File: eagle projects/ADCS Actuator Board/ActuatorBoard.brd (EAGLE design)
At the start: 91 x 91 mm, 278 parts, among them J19 TE_1-84953-1, J20 TE_1-84953-1, J21 TE_1-84953-1, U10 DRV10970_MOTOR_DRIVERDRV10970, U12 DRV10970_MOTOR_DRIVERDRV10970, U13 ADS7841E_2K5, U15 TLV9051IDCKR, U19 TLV9051IDCKR, U2 ADS7841E_2K5, U21 TLV9051IDCKR, U23 TLV9051IDCKR, U24 TLV9051IDCKR, U25 ADS7841E_2K5, U26 TLV9051IDCKR, U27 ADS7841E_2K5, U28 TLV9051IDCKR, U29 TLV9051IDCKR, U3 ADS7841E_2K5, U30 TLV9051IDCKR, U31 TLV9051IDCKR, U32 TLV9051IDCKR, U34 TVS991, U35 BD6210F-E2, U38 TVS991, U39 BD6210F-E2, U4 ADS7841E_2K5, U5 TVS991, U6 TLV9051IDCKR, U7 DRV10970_MOTOR_DRIVERDRV10970, U9 BD6210F-E2

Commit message: minor layout tweaks
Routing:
- net GND: vias 170 -> 172
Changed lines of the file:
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@@
 <setting verticaltext="up"/>
 </settings>
-<grid distance="1" unitdist="mil" unit="mil" style="lines" multiple="1" display="yes" altdistance="12.5" altunitdist="mil" altunit="mm"/>
+<grid distance="50" unitdist="mil" unit="mil" style="lines" multiple="1" display="yes" altdistance="12.5" altunitdist="mil" altunit="mil"/>
 <layers>
 <layer number="1" name="Top" color="4" fill="1" visible="yes" active="yes"/>
@@
 </layers>
 <board>
-<fusionsync huburn="a.YnVzaW5lc3M6bXlkYWwyMA" projecturn="a.YnVzaW5lc3M6bXlkYWwyMCMyMDIxMDExNjM3MjQwMzc3Ng" f3durn="urn:adsk.wipprod:dm.lineage:TKW3tc-mS0qsFWWO9AN0Ug" pcbguid="" lastpulledtime="" lastsyncedchangeguid="" latestrevisionid="0074a831-43cd-42bd-b3bd-cc89c6651567" lastsyncedrevisionid="0074a831-43cd-42bd-b3bd-cc89c6651567" lastboardhashguid="857bcac5-dcdf-7e34-be52-16fdd3c31308" lastpushedtime="2021-02-03T02:47:48Z" linktopcb3d="false"/>
+<fusionsync huburn="a.YnVzaW5lc3M6bXlkYWwyMA" projecturn="a.YnVzaW5lc3M6bXlkYWwyMCMyMDIxMDExNjM3MjQwMzc3Ng" f3durn="urn:adsk.wipprod:dm.lineage:TKW3tc-mS0qsFWWO9AN0Ug" pcbguid="" lastpulledtime="2021-02-14T18:09:55Z" lastsyncedchangeguid="" latestrevisionid="c2152030-a1ea-4700-91c3-66171d633219" lastsyncedrevisionid="c2152030-a1ea-4700-91c3-66171d633219" lastboardhashguid="a1286e25-3132-5004-a41b-18cce8fad25a" lastpushedtime="2021-02-14T18:11:04Z" linktopcb3d="true"/>
 <plain>
-<wire x1="0" y1="0" x2="31.5" y2="0" width="0.1524" layer="20" locked="yes"/>
-<wire x1="31.5" y1="0" x2="31.5" y2="7" width="0.1524" layer="20" locked="yes"/>
-<wire x1="31.5" y1="7" x2="59.5" y2="7" width="0.1524" layer="20" locked="yes"/>
-<wire x1="59.5" y1="7" x2="59.5" y2="0" width="0.1524" layer="20" locked="yes"/>
-<wire x1="59.5" y1="0" x2="91" y2="0" width="0.1524" layer="20" locked="yes"/>
-<wire x1="91" y1="0" x2="91" y2="42" width="0.1524" layer="20" locked="yes"/>
-<wire x1="91" y1="42" x2="87" y2="42" width="0.1524" layer="20" locked="yes"/>
-<wire x1="87" y1="42" x2="87" y2="80" width="0.1524" layer="20" locked="yes"/>
-<wire x1="87" y1="80" x2="91" y2="80" width="0.1524" layer="20" locked="yes"/>
-<wire x1="91" y1="80" x2="91" y2="91" width="0.1524" layer="20" locked="yes"/>
-<wire x1="91" y1="91" x2="0" y2="91" width="0.1524" layer="20" locked="yes"/>
-<wire x1="0" y1="91" x2="0" y2="80" width="0.1524" layer="20" locked="yes"/>
-<wire x1="0" y1="80" x2="4" y2="80" width="0.1524" layer="20" locked="yes"/>
-<wire x1="4" y1="80" x2="4" y2="42" width="0.1524" layer="20" locked="yes"/>
-<wire x1="4" y1="42" x2="0" y2="42" width="0.1524" layer="20" locked="yes"/>
-<wire x1="0" y1="42" x2="0" y2="0" width="0.1524" layer="20" locked="yes"/>
 <text x="64.6176" y="16.4719" size="1.016" layer="51" font="vector" rot="R90">ACTUATOR BOARD - REV A</text>
 <text x="65.9511" y="16.4719" size="1.016" layer="151" font="vector" rot="R90">Dalhousie Space Systems Lab</text>
@@
 <rectangle x1="72.6059" y1="66.3067" x2="73.2155" y2="66.3321" locked="yes" layer="203" rot="R180" grouprefs="BOTTOM_LOGO"/>
 <rectangle x1="72.8091" y1="66.3321" x2="73.0631" y2="66.3575" locked="yes" layer="203" rot="R180" grouprefs="BOTTOM_LOGO"/>
+<hole x="34.025" y="44.335" drill="2.5"/>
+<hole x="76.025" y="18.335" drill="2.5"/>
+<hole x="76.025" y="44.335" drill="2.5"/>
+<hole x="34.025" y="18.335" drill="2.5"/>
+<wire x1="0" y1="42" x2="0" y2="0" width="0.1524" layer="20"/>
+<wire x1="0" y1="0" x2="31.5" y2="0" width="0.1524" layer="20"/>
+<wire x1="31.5" y1="0" x2="31.5" y2="7" width="0.1524" layer="20"/>
+<wire x1="31.5" y1="7" x2="59.5" y2="7" width="0.1524" layer="20"/>
+<wire x1="59.5" y1="7" x2="59.5" y2="0" width="0.1524" layer="20"/>
+<wire x1="59.5" y1="0" x2="91" y2="0" width="0.1524" layer="20"/>
+<wire x1="91" y1="0" x2="91" y2="42" width="0.1524" layer="20"/>
+<wire x1="91" y1="42" x2="87" y2="42" width="0.1524" layer="20"/>
+<wire x1="87" y1="42" x2="87" y2="80" width="0.1524" layer="20"/>
+<wire x1="87" y1="80" x2="91" y2="80" width="0.1524" layer="20"/>
+<wire x1="91" y1="80" x2="91" y2="91" width="0.1524" layer="20"/>
+<wire x1="91" y1="91" x2="0" y2="91" width="0.1524" layer="20"/>
+<wire x1="0" y1="91" x2="0" y2="80" width="0.1524" layer="20"/>
+<wire x1="0" y1="80" x2="4" y2="80" width="0.1524" layer="20"/>
+<wire x1="4" y1="80" x2="4" y2="42" width="0.1524" layer="20"/>
+<wire x1="4" y1="42" x2="0" y2="42" width="0.1524" layer="20"/>
 </plain>
 <attributes>
@@
 <attribute name="MF" value="" x="6.985" y="45.72" size="1.778" layer="28" rot="MR270" display="off"/>
 <attribute name="MPN" value="" x="6.985" y="45.72" size="1.778" layer="28" rot="MR270" display="off"/>
-<attribute name="NAME" x="4.572" y="46.609" size="1.016" layer="26" rot="MR270"/>
+<attribute name="NAME" x="10.287" y="47.244" size="1.016" layer="26" rot="MR270"/>
 <attribute name="OC_FARNELL" value="unknown" x="6.985" y="45.72" size="1.778" layer="28" rot="MR270" display="off"/>
 <attribute name="OC_NEWARK" value="unknown" x="6.985" y="45.72" size="1.778" layer="28" rot="MR270" display="off"/>
@@
 <wire x1="11.43" y1="69.215" x2="12.065" y2="68.58" width="0.1524" layer="16"/>
 <wire x1="12.065" y1="68.58" x2="22.225" y2="68.58" width="0.1524" layer="16"/>
-<wire x1="22.225" y1="68.58" x2="30.48" y2="60.325" width="0.1524" layer="16"/>
+<wire x1="22.225" y1="68.58" x2="29.5275" y2="61.2775" width="0.1524" layer="16"/>
+<wire x1="29.5275" y1="61.2775" x2="30.1625" y2="60.6425" width="0.1524" layer="16"/>
+<wire x1="30.1625" y1="60.6425" x2="30.48" y2="60.325" width="0.1524" layer="16"/>
 <wire x1="30.48" y1="60.325" x2="30.48" y2="59.055" width="0.1524" layer="16"/>
 <wire x1="30.48" y1="59.055" x2="31.75" y2="57.785" width="0.1524" layer="16"/>
@@
 <wire x1="39.0525" y1="44.45" x2="39.0525" y2="56.1975" width="0.1524" layer="1"/>
 <wire x1="39.0525" y1="56.1975" x2="34.29" y2="60.96" width="0.1524" layer="1"/>
-<wire x1="34.29" y1="60.96" x2="28.2575" y2="60.96" width="0.1524" layer="1"/>
-<wire x1="28.2575" y1="60.96" x2="9.525" y2="79.6925" width="0.1524" layer="1"/>
+<wire x1="29.21" y1="60.96" x2="34.29" y2="60.96" width="0.1524" layer="1"/>
+<wire x1="9.525" y1="79.6925" x2="20.47875" y2="68.73875" width="0.1524" layer="1"/>
+<wire x1="20.47875" y1="68.73875" x2="21.43125" y2="68.73875" width="0.1524" layer="1"/>
+<wire x1="21.43125" y1="68.73875" x2="29.21" y2="60.96" width="0.1524" layer="1"/>
 </signal>
 <signal name="GND">
@@
 <via x="67.5206" y="87.0821" extent="1-16" drill="0.35"/>
 <via x="43.863940625" y="86.946059375" extent="1-16" drill="0.35"/>
+<via x="34.29" y="34.29" extent="1-16" drill="0.35"/>
+<via x="34.29" y="25.4" extent="1-16" drill="0.35"/>
 </signal>
 <signal name="+5V">
@@
 <wire x1="69.8218" y1="71.50365" x2="69.8218" y2="81.2518" width="0.1524" layer="1"/>
 <wire x1="69.85" y1="81.28" x2="70.53285" y2="80.59715" width="0.1524" layer="16"/>
-<wire x1="70.53285" y1="80.59715" x2="70.53285" y2="77.47" width="0.1524" layer="16"/>
-<wire x1="70.53285" y1="77.47" x2="70.53285" y2="77.1944125" width="0.1524" layer="16"/>
+<wire x1="70.53285" y1="80.59715" x2="70.53285" y2="77.1944125" width="0.1524" layer="16"/>
 <wire x1="70.53285" y1="77.1944125" x2="70.1809375" y2="76.8425" width="0.1524" layer="16"/>
 <wire x1="70.1809375" y1="76.8425" x2="69.5183" y2="76.8425" width="0.1524" layer="16"/>
@@
 <wire x1="43" y1="85.365" x2="42.89" y2="85.475" width="0.2" layer="1"/>
 <wire x1="42.89" y1="85.475" x2="42.89" y2="88.71" width="0.2" layer="1"/>
-<wire x1="47.69665" y1="73.73165" x2="47.69665" y2="80" width="0.2" layer="16"/>
+<wire x1="47.69665" y1="73.73165" x2="47.69665" y2="80.40045" width="0.2" layer="16"/>
 <wire x1="42.89" y1="88.71" x2="43.89" y2="88.71" width="0.2" layer="1"/>
-<wire x1="47.69665" y1="80" x2="47.69665" y2="80.40045" width="0.2" layer="16"/>
 <wire x1="43" y1="85.0971" x2="43" y2="85.365" width="0.2" layer="16"/>
 <wire x1="47.69665" y1="80.40045" x2="43" y2="85.0971" width="0.2" layer="16"/>
@@
 <wire x1="46.0756" y1="11.840325" x2="46.0756" y2="11.019675" width="0.1524" layer="1"/>
 <wire x1="45.085" y1="10.029075" x2="45.085" y2="8.89" width="0.1524" layer="1"/>
-<wire x1="46.0756" y1="11.840325" x2="45.7854625" y2="12.1304625" width="0.1524" layer="1"/>
+<wire x1="46.0756" y1="11.840325" x2="45.72" y2="12.195925" width="0.1524" layer="1"/>
 <wire x1="46.0756" y1="11.019675" x2="45.085" y2="10.029075" width="0.1524" layer="1"/>
 <contactref element="U3" pad="15"/>
@@
 <via x="45.72" y="20.32" extent="1-16" drill="0.35"/>
 <wire x1="45.72" y1="20.32" x2="45.72" y2="12.195925" width="0.1524" layer="1"/>
-<wire x1="45.72" y1="12.195925" x2="45.7854625" y2="12.1304625" width="0.1524" layer="1"/>
 </signal>
 <signal name="!CS!_CUR_SENSE_MAG">

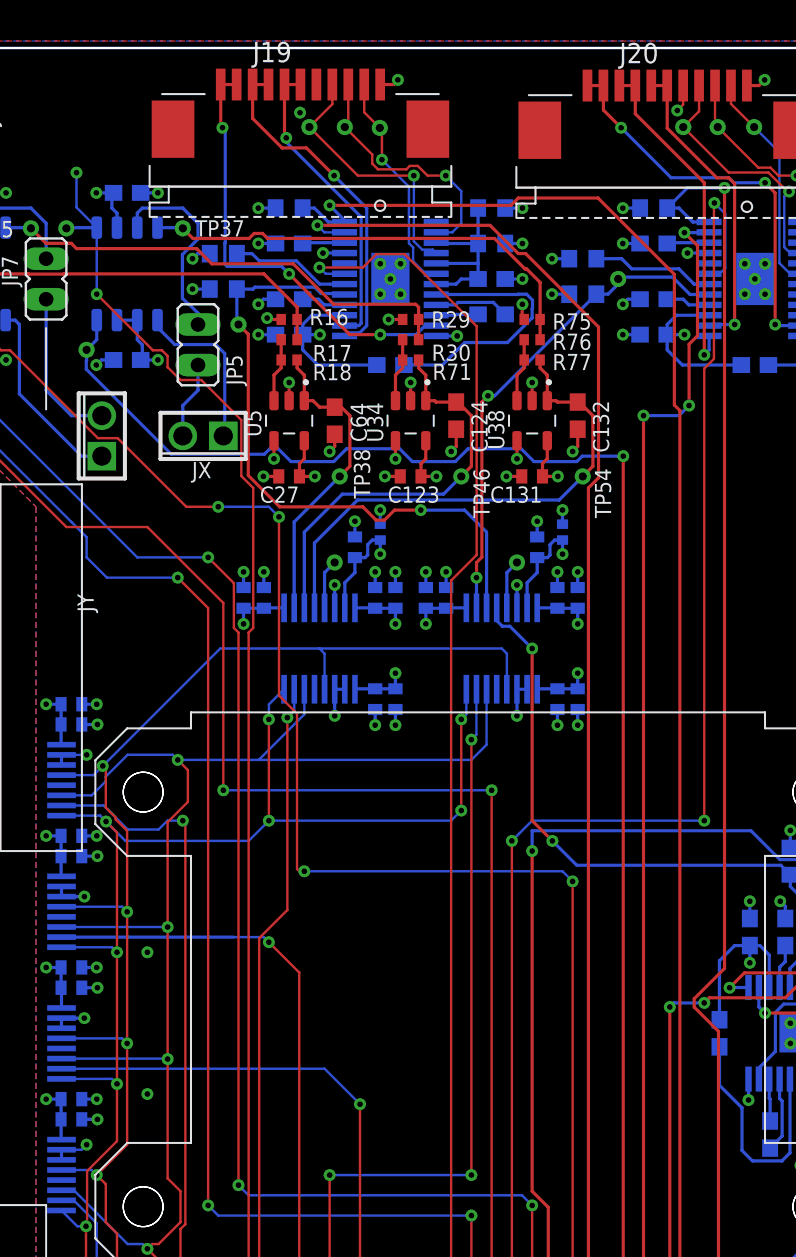
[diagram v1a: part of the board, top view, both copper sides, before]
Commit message: filled in ground spots and rearranged designators
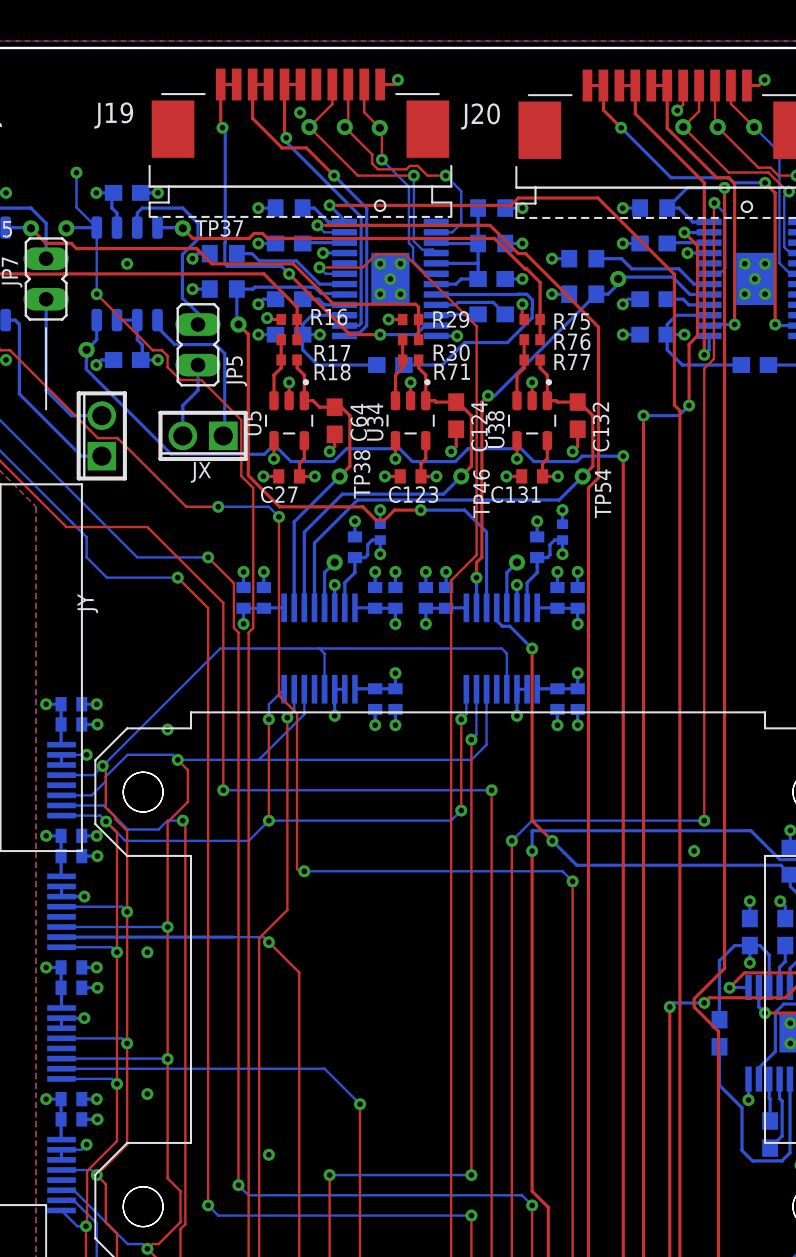
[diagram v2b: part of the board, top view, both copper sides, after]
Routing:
- net GND: vias 172 -> 176
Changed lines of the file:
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@@
 </layers>
 <board>
-<fusionsync huburn="a.YnVzaW5lc3M6bXlkYWwyMA" projecturn="a.YnVzaW5lc3M6bXlkYWwyMCMyMDIxMDExNjM3MjQwMzc3Ng" f3durn="urn:adsk.wipprod:dm.lineage:TKW3tc-mS0qsFWWO9AN0Ug" pcbguid="" lastpulledtime="2021-02-14T18:09:55Z" lastsyncedchangeguid="" latestrevisionid="c2152030-a1ea-4700-91c3-66171d633219" lastsyncedrevisionid="c2152030-a1ea-4700-91c3-66171d633219" lastboardhashguid="a1286e25-3132-5004-a41b-18cce8fad25a" lastpushedtime="2021-02-14T18:11:04Z" linktopcb3d="true"/>
+<fusionsync huburn="a.YnVzaW5lc3M6bXlkYWwyMA" projecturn="a.YnVzaW5lc3M6bXlkYWwyMCMyMDIxMDExNjM3MjQwMzc3Ng" f3durn="urn:adsk.wipprod:dm.lineage:TKW3tc-mS0qsFWWO9AN0Ug" pcbguid="" lastpulledtime="2021-02-14T18:09:55Z" lastsyncedchangeguid="" latestrevisionid="c2152030-a1ea-4700-91c3-66171d633219" lastsyncedrevisionid="c2152030-a1ea-4700-91c3-66171d633219" lastboardhashguid="a1286e25-3132-5004-a41b-18cce8fad25a" lastpushedtime="2021-02-14T18:11:04Z" linktopcb3d="false"/>
 <plain>
 <text x="64.6176" y="16.4719" size="1.016" layer="51" font="vector" rot="R90">ACTUATOR BOARD - REV A</text>
@@
 <wire x1="4" y1="80" x2="4" y2="42" width="0.1524" layer="20"/>
 <wire x1="4" y1="42" x2="0" y2="42" width="0.1524" layer="20"/>
+<text x="111.6076" y="30.4419" size="1.016" layer="51" font="vector" rot="R90">ACTUATOR BOARD - REV A</text>
+<text x="112.9411" y="30.4419" size="1.016" layer="151" font="vector" rot="R90">Dalhousie Space Systems Lab</text>
+<text x="110.2233" y="30.4165" size="1.016" layer="51" font="vector" rot="R90">LORIS CubeSat ADCS Subsystem</text>
+<text x="115.7605" y="30.4419" size="1.016" layer="51" font="vector" rot="R90">J. Smith, C. Mattatall, T. Christison</text>
+<text x="114.3" y="30.4419" size="1.016" layer="51" font="vector" rot="R90">Designers:</text>
 </plain>
 <attributes>
@@
 <attribute name="MF" value="" x="13.0175" y="2.8575" size="1.778" layer="28" rot="MR180" display="off"/>
 <attribute name="MPN" value="" x="13.0175" y="2.8575" size="1.778" layer="28" rot="MR180" display="off"/>
-<attribute name="NAME" x="10.2235" y="1.0795" size="1.27" layer="26" rot="MR180"/>
+<attribute name="NAME" x="3.8735" y="2.3495" size="1.27" layer="26" rot="MR180"/>
 <attribute name="OC_FARNELL" value="unknown" x="13.0175" y="2.8575" size="1.778" layer="28" rot="MR180" display="off"/>
 <attribute name="OC_NEWARK" value="unknown" x="13.0175" y="2.8575" size="1.778" layer="28" rot="MR180" display="off"/>
@@
 <attribute name="MF" value="" x="18.7325" y="2.8575" size="1.778" layer="28" rot="MR180" display="off"/>
 <attribute name="MPN" value="" x="18.7325" y="2.8575" size="1.778" layer="28" rot="MR180" display="off"/>
-<attribute name="NAME" x="15.9385" y="1.0795" size="1.27" layer="26" rot="MR180"/>
+<attribute name="NAME" x="7.0485" y="2.3495" size="1.27" layer="26" rot="MR180"/>
 <attribute name="OC_FARNELL" value="unknown" x="18.7325" y="2.8575" size="1.778" layer="28" rot="MR180" display="off"/>
 <attribute name="OC_NEWARK" value="unknown" x="18.7325" y="2.8575" size="1.778" layer="28" rot="MR180" display="off"/>
@@
 <attribute name="MF" value="" x="24.4475" y="2.8575" size="1.778" layer="28" rot="MR180" display="off"/>
 <attribute name="MPN" value="" x="24.4475" y="2.8575" size="1.778" layer="28" rot="MR180" display="off"/>
-<attribute name="NAME" x="21.6535" y="1.0795" size="1.27" layer="26" rot="MR180"/>
+<attribute name="NAME" x="28.0035" y="2.3495" size="1.27" layer="26" rot="MR180"/>
 <attribute name="OC_FARNELL" value="unknown" x="24.4475" y="2.8575" size="1.778" layer="28" rot="MR180" display="off"/>
 <attribute name="OC_NEWARK" value="unknown" x="24.4475" y="2.8575" size="1.778" layer="28" rot="MR180" display="off"/>
@@
 <attribute name="MF" value="" x="2.8575" y="38.735" size="1.778" layer="28" rot="MR270" display="off"/>
 <attribute name="MPN" value="" x="2.8575" y="38.735" size="1.778" layer="28" rot="MR270" display="off"/>
-<attribute name="NAME" x="1.0795" y="39.624" size="1.016" layer="26" rot="MR270"/>
+<attribute name="NAME" x="0.381" y="12.192" size="1.016" layer="26" rot="MR180"/>
 <attribute name="OC_FARNELL" value="unknown" x="2.8575" y="38.735" size="1.778" layer="28" rot="MR270" display="off"/>
 <attribute name="OC_NEWARK" value="unknown" x="2.8575" y="38.735" size="1.778" layer="28" rot="MR270" display="off"/>
@@
 <attribute name="MF" value="" x="2.8575" y="33.02" size="1.778" layer="28" rot="MR270" display="off"/>
 <attribute name="MPN" value="" x="2.8575" y="33.02" size="1.778" layer="28" rot="MR270" display="off"/>
-<attribute name="NAME" x="1.0795" y="33.909" size="1.016" layer="26" rot="MR270"/>
+<attribute name="NAME" x="0.381" y="9.9695" size="1.016" layer="26" rot="MR180"/>
 <attribute name="OC_FARNELL" value="unknown" x="2.8575" y="33.02" size="1.778" layer="28" rot="MR270" display="off"/>
 <attribute name="OC_NEWARK" value="unknown" x="2.8575" y="33.02" size="1.778" layer="28" rot="MR270" display="off"/>
@@
 <attribute name="MF" value="" x="2.8575" y="27.305" size="1.778" layer="28" rot="MR270" display="off"/>
 <attribute name="MPN" value="" x="2.8575" y="27.305" size="1.778" layer="28" rot="MR270" display="off"/>
-<attribute name="NAME" x="1.0795" y="28.194" size="1.016" layer="26" rot="MR270"/>
+<attribute name="NAME" x="0.381" y="7.747" size="1.016" layer="26" rot="MR180"/>
 <attribute name="OC_FARNELL" value="unknown" x="2.8575" y="27.305" size="1.778" layer="28" rot="MR270" display="off"/>
 <attribute name="OC_NEWARK" value="unknown" x="2.8575" y="27.305" size="1.778" layer="28" rot="MR270" display="off"/>
@@
 <attribute name="MF" value="" x="2.8575" y="21.2725" size="1.778" layer="28" rot="MR270" display="off"/>
 <attribute name="MPN" value="" x="2.8575" y="21.2725" size="1.778" layer="28" rot="MR270" display="off"/>
-<attribute name="NAME" x="1.0795" y="22.1615" size="1.016" layer="26" rot="MR270"/>
+<attribute name="NAME" x="0.381" y="5.5245" size="1.016" layer="26" rot="MR180"/>
 <attribute name="OC_FARNELL" value="unknown" x="2.8575" y="21.2725" size="1.778" layer="28" rot="MR270" display="off"/>
 <attribute name="OC_NEWARK" value="unknown" x="2.8575" y="21.2725" size="1.778" layer="28" rot="MR270" display="off"/>
@@
 <attribute name="MF" value="" x="2.8575" y="15.5575" size="1.778" layer="28" rot="MR270" display="off"/>
 <attribute name="MPN" value="" x="2.8575" y="15.5575" size="1.778" layer="28" rot="MR270" display="off"/>
-<attribute name="NAME" x="1.0795" y="16.4465" size="1.016" layer="26" rot="MR270"/>
+<attribute name="NAME" x="0.381" y="3.302" size="1.016" layer="26" rot="MR180"/>
 <attribute name="OC_FARNELL" value="unknown" x="2.8575" y="15.5575" size="1.778" layer="28" rot="MR270" display="off"/>
 <attribute name="OC_NEWARK" value="unknown" x="2.8575" y="15.5575" size="1.778" layer="28" rot="MR270" display="off"/>
@@
 </element>
 <element name="J19" library="my_library" library_urn="urn:adsk.eagle:library:22876504" package="TE_1-84953-1" package3d_urn="urn:adsk.eagle:package:26760321/5" value="TE_1-84953-1" x="43.89" y="84.11" smashed="yes">
-<attribute name="NAME" x="40.89" y="90.11" size="1.27" layer="25" ratio="10"/>
+<attribute name="NAME" x="31.0475" y="86.3" size="1.27" layer="25" ratio="10"/>
 </element>
 <element name="J20" library="my_library" library_urn="urn:adsk.eagle:library:22876504" package="TE_1-84953-1" package3d_urn="urn:adsk.eagle:package:26760321/5" value="TE_1-84953-1" x="66.89" y="84.045" smashed="yes">
-<attribute name="NAME" x="63.89" y="90.045" size="1.27" layer="25" ratio="10"/>
+<attribute name="NAME" x="54.0475" y="86.235" size="1.27" layer="25" ratio="10"/>
 </element>
 <element name="J21" library="my_library" library_urn="urn:adsk.eagle:library:22876504" package="TE_1-84953-1" package3d_urn="urn:adsk.eagle:package:26760321/5" value="TE_1-84953-1" x="83.98" y="29.11" smashed="yes" rot="R270">
@@
 <via x="34.29" y="34.29" extent="1-16" drill="0.35"/>
 <via x="34.29" y="25.4" extent="1-16" drill="0.35"/>
+<via x="41.91" y="21.59" extent="1-16" drill="0.35"/>
+<via x="33.02" y="77.47" extent="1-16" drill="0.35"/>
+<via x="68.58" y="40.64" extent="1-16" drill="0.35"/>
+<via x="35.56" y="48.26" extent="1-16" drill="0.35"/>
 </signal>
 <signal name="+5V">
